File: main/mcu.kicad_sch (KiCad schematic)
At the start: 13 parts, among them J1201 Conn_ARM_JTAG_SWD_20, SW1201 B3SL-1022P, U1201 STM32L476RGTx, Y1201 8MHz

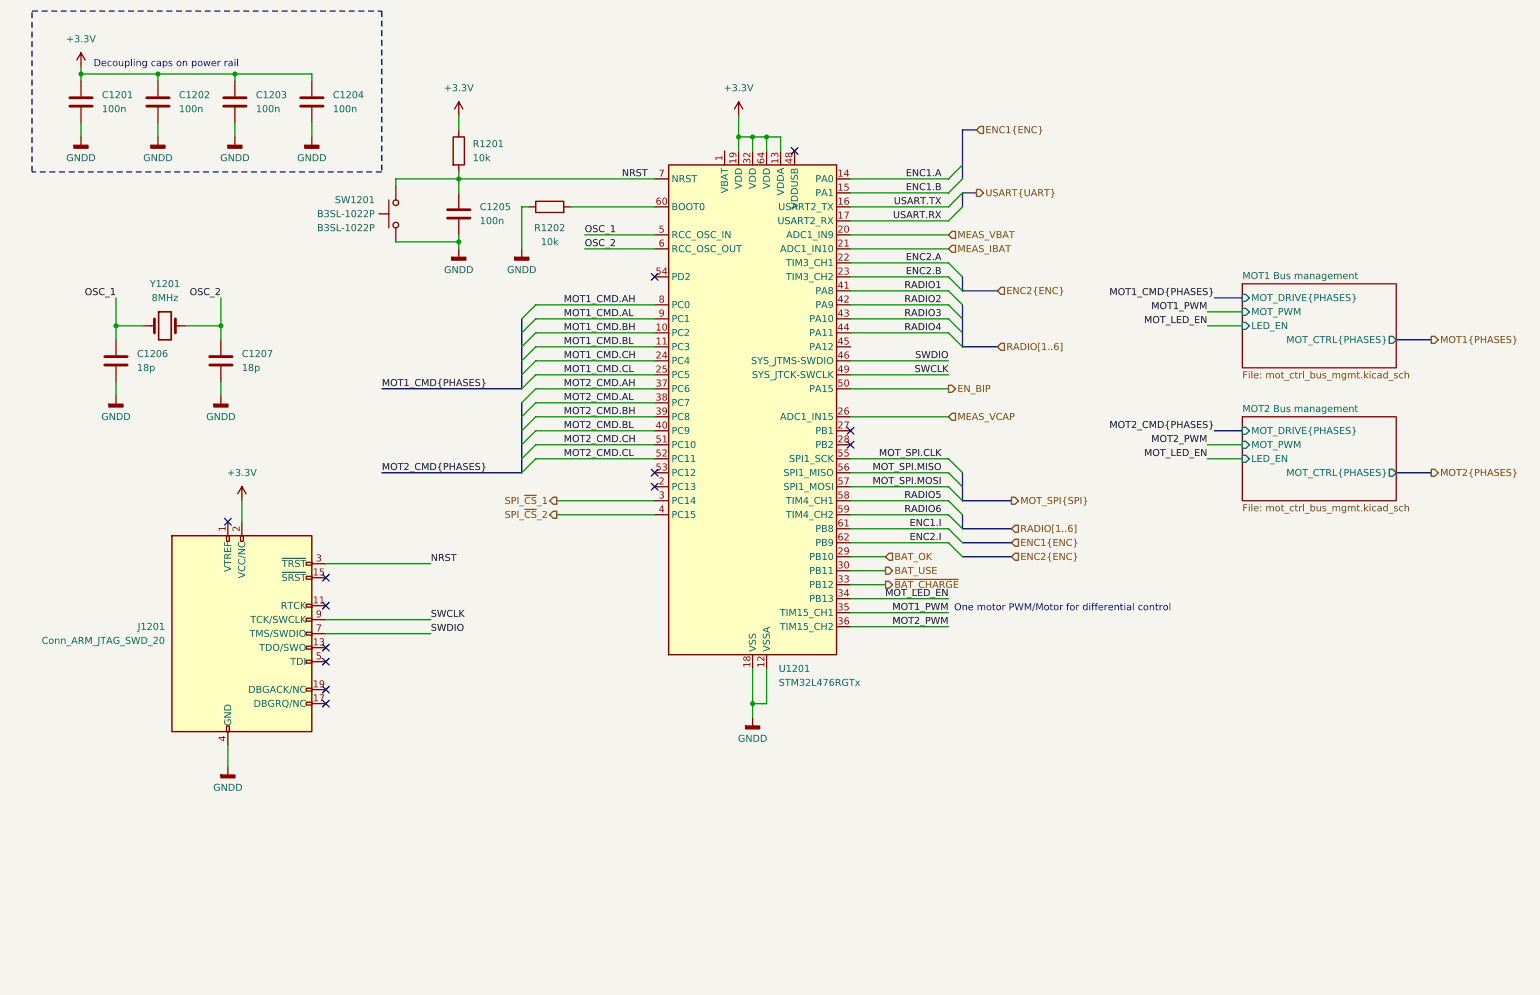
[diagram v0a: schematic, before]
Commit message: Clean silkscreen
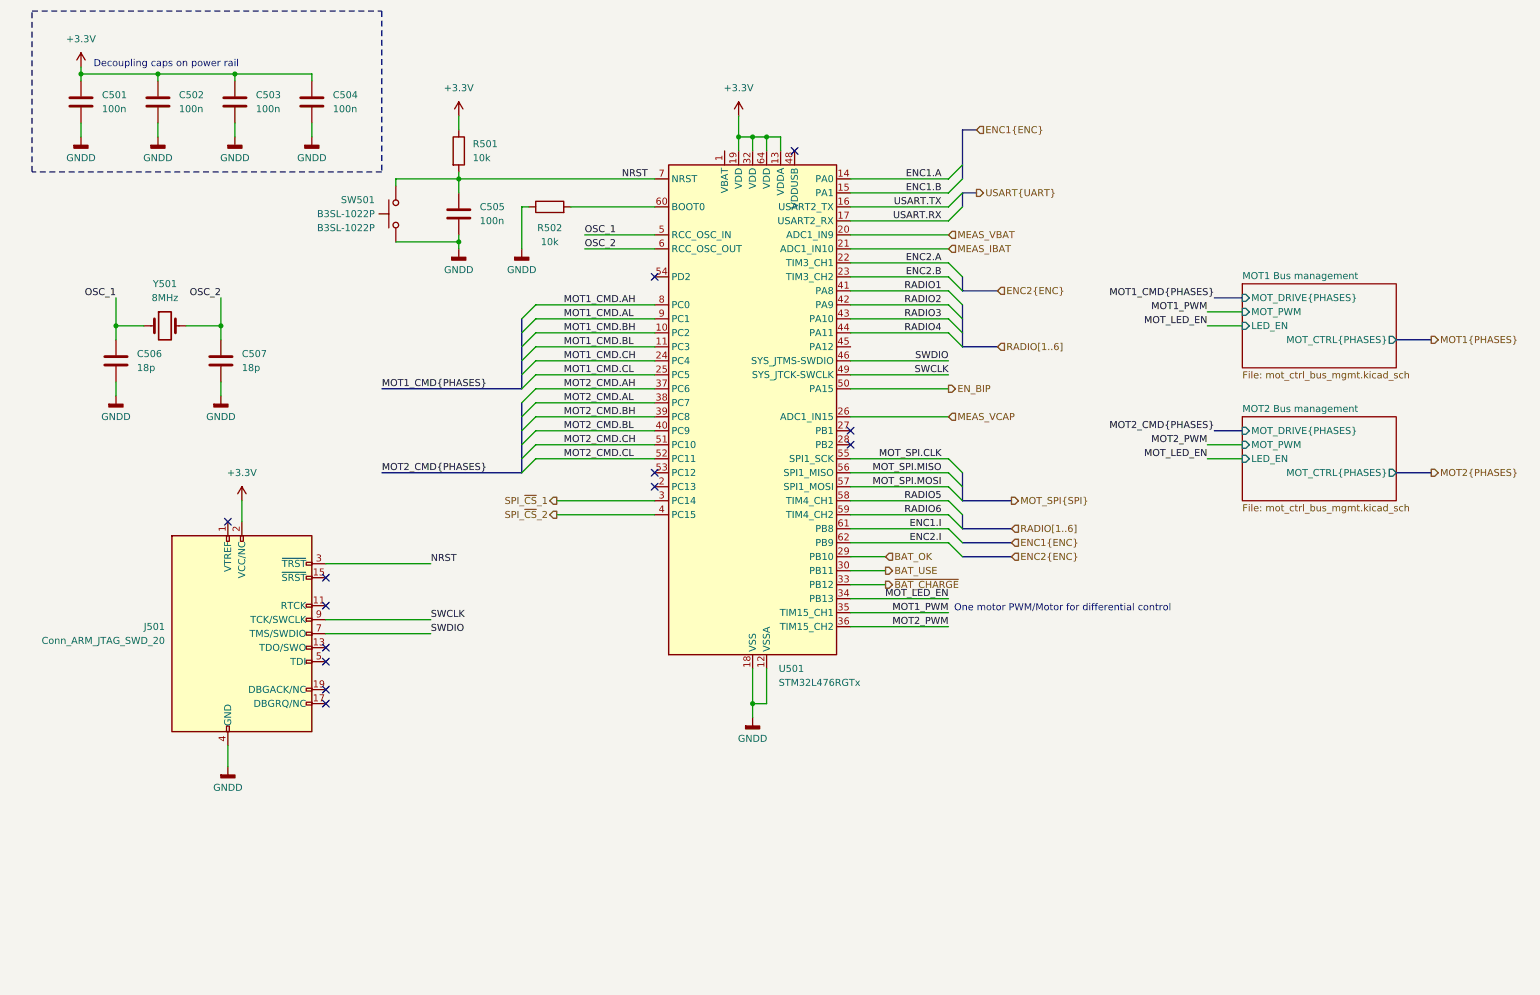
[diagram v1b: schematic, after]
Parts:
- renumbered C1201 to C501, C1202 to C502, C1203 to C503, C1204 to C504, C1205 to C505, C1206 to C506, C1207 to C507, J1201 to J501, R1201 to R501, R1202 to R502, SW1201 to SW501, U1201 to U501, Y1201 to Y501
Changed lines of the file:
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@@
 	(label "ENC2.I"
 		(at 177.8 109.22 180)
+		(fields_autoplaced yes)
 		(effects
 			(font
@@
 	(label "ENC1.I"
 		(at 177.8 106.68 180)
+		(fields_autoplaced yes)
 		(effects
 			(font
@@
 		(dnp no)
 		(fields_autoplaced yes)
-		(property "Reference" "SW1201"
+		(property "Reference" "SW501"
 			(at 74.93 46.9899 90)
 			(effects
@@
 			(project "dsv4"
 				(path "/c07e9297-fde8-4755-803e-d05072cd6096/0865f076-bf0e-442f-8617-d4097538e68b"
-					(reference "SW1201")
+					(reference "SW501")
 					(unit 1)
 				)
@@
 		(dnp no)
 		(fields_autoplaced yes)
-		(property "Reference" "C1204"
+		(property "Reference" "C504"
 			(at 67.31 27.9399 0)
 			(effects
@@
 			(project "dsv4"
 				(path "/c07e9297-fde8-4755-803e-d05072cd6096/0865f076-bf0e-442f-8617-d4097538e68b"
-					(reference "C1204")
+					(reference "C504")
 					(unit 1)
 				)
@@
 		(dnp no)
 		(fields_autoplaced yes)
-		(property "Reference" "#PWR01213"
+		(property "Reference" "#PWR0513"
 			(at 143.51 147.32 0)
 			(effects
@@
 			(project "dsv4"
 				(path "/c07e9297-fde8-4755-803e-d05072cd6096/0865f076-bf0e-442f-8617-d4097538e68b"
-					(reference "#PWR01213")
+					(reference "#PWR0513")
 					(unit 1)
 				)
@@
 		(dnp no)
 		(fields_autoplaced yes)
-		(property "Reference" "#PWR01210"
+		(property "Reference" "#PWR0510"
 			(at 27.94 88.9 0)
 			(effects
@@
 			(project "dsv4"
 				(path "/c07e9297-fde8-4755-803e-d05072cd6096/0865f076-bf0e-442f-8617-d4097538e68b"
-					(reference "#PWR01210")
+					(reference "#PWR0510")
 					(unit 1)
 				)
@@
 		(dnp no)
 		(fields_autoplaced yes)
-		(property "Reference" "#PWR01211"
+		(property "Reference" "#PWR0511"
 			(at 46.99 88.9 0)
 			(effects
@@
 			(project "dsv4"
 				(path "/c07e9297-fde8-4755-803e-d05072cd6096/0865f076-bf0e-442f-8617-d4097538e68b"
-					(reference "#PWR01211")
+					(reference "#PWR0511")
 					(unit 1)
 				)
@@
 		(dnp no)
 		(fields_autoplaced yes)
-		(property "Reference" "C1207"
+		(property "Reference" "C507"
 			(at 50.8 74.9299 0)
 			(effects
@@
 			(project "dsv4"
 				(path "/c07e9297-fde8-4755-803e-d05072cd6096/0865f076-bf0e-442f-8617-d4097538e68b"
-					(reference "C1207")
+					(reference "C507")
 					(unit 1)
 				)
@@
 		(dnp no)
 		(fields_autoplaced yes)
-		(property "Reference" "J1201"
+		(property "Reference" "J501"
 			(at 36.83 124.4599 0)
 			(effects
@@
 			(project "dsv4"
 				(path "/c07e9297-fde8-4755-803e-d05072cd6096/0865f076-bf0e-442f-8617-d4097538e68b"
-					(reference "J1201")
+					(reference "J501")
 					(unit 1)
 				)
@@
 		(dnp no)
 		(fields_autoplaced yes)
-		(property "Reference" "#PWR01209"
+		(property "Reference" "#PWR0509"
 			(at 101.6 62.23 0)
 			(effects
@@
 			(project "dsv4"
 				(path "/c07e9297-fde8-4755-803e-d05072cd6096/0865f076-bf0e-442f-8617-d4097538e68b"
-					(reference "#PWR01209")
+					(reference "#PWR0509")
 					(unit 1)
 				)
@@
 		(dnp no)
 		(fields_autoplaced yes)
-		(property "Reference" "C1206"
+		(property "Reference" "C506"
 			(at 31.75 74.9299 0)
 			(effects
@@
 			(project "dsv4"
 				(path "/c07e9297-fde8-4755-803e-d05072cd6096/0865f076-bf0e-442f-8617-d4097538e68b"
-					(reference "C1206")
+					(reference "C506")
 					(unit 1)
 				)
@@
 		(dnp no)
 		(fields_autoplaced yes)
-		(property "Reference" "R1202"
+		(property "Reference" "R502"
 			(at 106.68 52.07 90)
 			(effects
@@
 			(project "dsv4"
 				(path "/c07e9297-fde8-4755-803e-d05072cd6096/0865f076-bf0e-442f-8617-d4097538e68b"
-					(reference "R1202")
+					(reference "R502")
 					(unit 1)
 				)
@@
 		(dnp no)
 		(fields_autoplaced yes)
-		(property "Reference" "R1201"
+		(property "Reference" "R501"
 			(at 92.71 36.8299 0)
 			(effects
@@
 			(project "dsv4"
 				(path "/c07e9297-fde8-4755-803e-d05072cd6096/0865f076-bf0e-442f-8617-d4097538e68b"
-					(reference "R1201")
+					(reference "R501")
 					(unit 1)
 				)
@@
 		(dnp no)
 		(fields_autoplaced yes)
-		(property "Reference" "#PWR01207"
+		(property "Reference" "#PWR0507"
 			(at 63.5 41.91 0)
 			(effects
@@
 			(project "dsv4"
 				(path "/c07e9297-fde8-4755-803e-d05072cd6096/0865f076-bf0e-442f-8617-d4097538e68b"
-					(reference "#PWR01207")
+					(reference "#PWR0507")
 					(unit 1)
 				)
@@
 		(dnp no)
 		(fields_autoplaced yes)
-		(property "Reference" "#PWR01204"
+		(property "Reference" "#PWR0504"
 			(at 21.59 41.91 0)
 			(effects
@@
 			(project "dsv4"
 				(path "/c07e9297-fde8-4755-803e-d05072cd6096/0865f076-bf0e-442f-8617-d4097538e68b"
-					(reference "#PWR01204")
+					(reference "#PWR0504")
 					(unit 1)
 				)
@@
 		(dnp no)
 		(fields_autoplaced yes)
-		(property "Reference" "#PWR01202"
+		(property "Reference" "#PWR0502"
 			(at 90.17 35.56 0)
 			(effects
@@
 			(project "dsv4"
 				(path "/c07e9297-fde8-4755-803e-d05072cd6096/0865f076-bf0e-442f-8617-d4097538e68b"
-					(reference "#PWR01202")
+					(reference "#PWR0502")
 					(unit 1)
 				)
@@
 		(dnp no)
 		(fields_autoplaced yes)
-		(property "Reference" "#PWR01201"
+		(property "Reference" "#PWR0501"
 			(at 21.59 26.67 0)
 			(effects
@@
 			(project "dsv4"
 				(path "/c07e9297-fde8-4755-803e-d05072cd6096/0865f076-bf0e-442f-8617-d4097538e68b"
-					(reference "#PWR01201")
+					(reference "#PWR0501")
 					(unit 1)
 				)
@@
 		(dnp no)
 		(fields_autoplaced yes)
-		(property "Reference" "#PWR01206"
+		(property "Reference" "#PWR0506"
 			(at 49.53 41.91 0)
 			(effects
@@
 			(project "dsv4"
 				(path "/c07e9297-fde8-4755-803e-d05072cd6096/0865f076-bf0e-442f-8617-d4097538e68b"
-					(reference "#PWR01206")
+					(reference "#PWR0506")
 					(unit 1)
 				)
@@
 		(dnp no)
 		(fields_autoplaced yes)
-		(property "Reference" "C1202"
+		(property "Reference" "C502"
 			(at 39.37 27.9399 0)
 			(effects
@@
 			(project "dsv4"
 				(path "/c07e9297-fde8-4755-803e-d05072cd6096/0865f076-bf0e-442f-8617-d4097538e68b"
-					(reference "C1202")
+					(reference "C502")
 					(unit 1)
 				)
@@
 		(dnp no)
 		(fields_autoplaced yes)
-		(property "Reference" "Y1201"
+		(property "Reference" "Y501"
 			(at 36.83 62.23 0)
 			(effects
@@
 			(project "dsv4"
 				(path "/c07e9297-fde8-4755-803e-d05072cd6096/0865f076-bf0e-442f-8617-d4097538e68b"
-					(reference "Y1201")
+					(reference "Y501")
 					(unit 1)
 				)
@@
 		(dnp no)
 		(fields_autoplaced yes)
-		(property "Reference" "#PWR01214"
+		(property "Reference" "#PWR0514"
 			(at 48.26 156.21 0)
 			(effects
@@
 			(project "dsv4"
 				(path "/c07e9297-fde8-4755-803e-d05072cd6096/0865f076-bf0e-442f-8617-d4097538e68b"
-					(reference "#PWR01214")
+					(reference "#PWR0514")
 					(unit 1)
 				)
@@
 		(dnp no)
 		(fields_autoplaced yes)
-		(property "Reference" "#PWR01212"
+		(property "Reference" "#PWR0512"
 			(at 50.8 105.41 0)
 			(effects
@@
 			(project "dsv4"
 				(path "/c07e9297-fde8-4755-803e-d05072cd6096/0865f076-bf0e-442f-8617-d4097538e68b"
-					(reference "#PWR01212")
+					(reference "#PWR0512")
 					(unit 1)
 				)
@@
 		(dnp no)
 		(fields_autoplaced yes)
-		(property "Reference" "C1205"
+		(property "Reference" "C505"
 			(at 93.98 48.2599 0)
 			(effects
@@
 			(project "dsv4"
 				(path "/c07e9297-fde8-4755-803e-d05072cd6096/0865f076-bf0e-442f-8617-d4097538e68b"
-					(reference "C1205")
+					(reference "C505")
 					(unit 1)
 				)
@@
 		(dnp no)
 		(fields_autoplaced yes)
-		(property "Reference" "#PWR01205"
+		(property "Reference" "#PWR0505"
 			(at 35.56 41.91 0)
 			(effects
@@
 			(project "dsv4"
 				(path "/c07e9297-fde8-4755-803e-d05072cd6096/0865f076-bf0e-442f-8617-d4097538e68b"
-					(reference "#PWR01205")
+					(reference "#PWR0505")
 					(unit 1)
 				)
@@
 		(dnp no)
 		(fields_autoplaced yes)
-		(property "Reference" "U1201"
+		(property "Reference" "U501"
 			(at 148.2441 132.08 0)
 			(effects
@@
 			(project "dsv4"
 				(path "/c07e9297-fde8-4755-803e-d05072cd6096/0865f076-bf0e-442f-8617-d4097538e68b"
-					(reference "U1201")
+					(reference "U501")
 					(unit 1)
 				)
@@
 		(dnp no)
 		(fields_autoplaced yes)
-		(property "Reference" "C1203"
+		(property "Reference" "C503"
 			(at 53.34 27.9399 0)
 			(effects
@@
 			(project "dsv4"
 				(path "/c07e9297-fde8-4755-803e-d05072cd6096/0865f076-bf0e-442f-8617-d4097538e68b"
-					(reference "C1203")
+					(reference "C503")
 					(unit 1)
 				)
@@
 		(dnp no)
 		(fields_autoplaced yes)
-		(property "Reference" "#PWR01208"
+		(property "Reference" "#PWR0508"
 			(at 90.17 62.23 0)
 			(effects
@@
 			(project "dsv4"
 				(path "/c07e9297-fde8-4755-803e-d05072cd6096/0865f076-bf0e-442f-8617-d4097538e68b"
-					(reference "#PWR01208")
+					(reference "#PWR0508")
 					(unit 1)
 				)
@@
 		(dnp no)
 		(fields_autoplaced yes)
-		(property "Reference" "C1201"
+		(property "Reference" "C501"
 			(at 25.4 27.9399 0)
 			(effects
@@
 			(project "dsv4"
 				(path "/c07e9297-fde8-4755-803e-d05072cd6096/0865f076-bf0e-442f-8617-d4097538e68b"
-					(reference "C1201")
+					(reference "C501")
 					(unit 1)
 				)
@@
 		(dnp no)
 		(fields_autoplaced yes)
-		(property "Reference" "#PWR01203"
+		(property "Reference" "#PWR0503"
 			(at 140.97 35.56 0)
 			(effects
@@
 			(project "dsv4"
 				(path "/c07e9297-fde8-4755-803e-d05072cd6096/0865f076-bf0e-442f-8617-d4097538e68b"
-					(reference "#PWR01203")
+					(reference "#PWR0503")
 					(unit 1)
 				)
@@
 			(project "dsv4"
 				(path "/c07e9297-fde8-4755-803e-d05072cd6096/0865f076-bf0e-442f-8617-d4097538e68b"
-					(page "11")
+					(page "16")
 				)
 			)
@@
 			(project "dsv4"
 				(path "/c07e9297-fde8-4755-803e-d05072cd6096/0865f076-bf0e-442f-8617-d4097538e68b"
-					(page "14")
-				)
-			)
+					(page "15")
+				)
+			)

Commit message: Tapeout
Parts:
- added D501: RED, LED_SMD:LED_0805_2012Metric, symbol Device:LED
- added J502: Debug, Connector_IDC:IDC-Header_2x10_P2.54mm_Vertical, symbol Connector_Generic:Conn_02x10_Odd_Even
- added R503: 3k3, Resistor_SMD:R_0805_2012Metric, symbol Device:R
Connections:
- net ENC1.A: now also J502.19 (Pin_19)
- net ENC1.B: now also J502.12 (Pin_12)
- net ENC1.I: now also J502.16 (Pin_16)
- net GNDD: now also D501.1 (K), J502.14 (Pin_14), J502.18 (Pin_18), J502.4 (Pin_4), J502.8 (Pin_8)
- net MOT1_CMD.AH: now also J502.1 (Pin_1)
- net MOT1_CMD.AL: now also J502.3 (Pin_3)
- net MOT1_CMD.BH: now also J502.5 (Pin_5)
- net MOT1_CMD.BL: now also J502.7 (Pin_7)
- net MOT1_CMD.CH: now also J502.9 (Pin_9)
- net MOT1_CMD.CL: now also J502.2 (Pin_2)
- net MOT1_PWM: now also J502.20 (Pin_20)
- net MOT2_CMD.AH: now also J502.6 (Pin_6)
- net MOT2_CMD.AL: now also J502.10 (Pin_10)
- net MOT2_CMD.BH: now also J502.11 (Pin_11)
- net MOT2_CMD.BL: now also J502.13 (Pin_13)
- net MOT2_CMD.CH: now also J502.15 (Pin_15)
- net MOT2_CMD.CL: now also J502.17 (Pin_17)
- net USER_LED: now reaches U501.28 (PB2)
- net USER_LED: now also R503.1
- new net: D501.2 (A), R503.2
- no-connect marks 13 -> 12
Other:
- note added: "DEBUG0"
- note added: "DEBUG1"
- note added: "DEBUG10"
- note added: "DEBUG11"
- note added: "DEBUG12"
- note added: "DEBUG13"
- note added: "DEBUG14"
- note added: "DEBUG15"
- note added: "DEBUG2"
- note added: "DEBUG3"
- note added: "DEBUG4"
- note added: "DEBUG5"
- note added: "DEBUG6"
- note added: "DEBUG7"
- note added: "DEBUG8"
- note added: "DEBUG9"

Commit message: Sent to fab
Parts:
- C501, C502, C503, C504, C505: MPN (none) -> CL21B104KACNFNC; Mouser SKU (none) -> 187-CL21B104KACNFNC
- C506, C507: MPN (none) -> GRM21A5C2J180FWA1D; Mouser SKU (none) -> 81-GRM21A5C2J180FWAD
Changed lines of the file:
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@@
+			)
+		)
+		(property "Quantity" ""
+			(at 78.74 49.53 0)
+			(effects
+				(font
+					(size 1.27 1.27)
+				)
 			)
 		)
@@
 			)
 		)
+		(property "MPN" "CL21B104KACNFNC "
+			(at 63.5 29.21 0)
+			(effects
+				(font
+					(size 1.27 1.27)
+				)
+			)
+		)
+		(property "Mouser SKU" " 187-CL21B104KACNFNC "
+			(at 63.5 29.21 0)
+			(effects
+				(font
+					(size 1.27 1.27)
+				)
+			)
+		)
+		(property "Quantity" ""
+			(at 63.5 29.21 0)
+			(effects
+				(font
+					(size 1.27 1.27)
+				)
+			)
+		)
 		(pin "1"
 		)
@@
 				)
 				(hide yes)
+			)
+		)
+		(property "Quantity" ""
+			(at 241.3 118.11 0)
+			(effects
+				(font
+					(size 1.27 1.27)
+				)
 			)
 		)
@@
 			)
 		)
+		(property "MPN" "GRM21A5C2J180FWA1D"
+			(at 46.99 76.2 0)
+			(effects
+				(font
+					(size 1.27 1.27)
+				)
+			)
+		)
+		(property "Mouser SKU" " 81-GRM21A5C2J180FWAD "
+			(at 46.99 76.2 0)
+			(effects
+				(font
+					(size 1.27 1.27)
+				)
+			)
+		)
+		(property "Quantity" ""
+			(at 46.99 76.2 0)
+			(effects
+				(font
+					(size 1.27 1.27)
+				)
+			)
+		)
 		(pin "1"
 		)
@@
 			)
 		)
+		(property "Quantity" ""
+			(at 50.8 125.73 0)
+			(effects
+				(font
+					(size 1.27 1.27)
+				)
+			)
+		)
 		(pin "8"
 		)
@@
 			)
 		)
+		(property "MPN" "GRM21A5C2J180FWA1D"
+			(at 27.94 76.2 0)
+			(effects
+				(font
+					(size 1.27 1.27)
+				)
+			)
+		)
+		(property "Mouser SKU" " 81-GRM21A5C2J180FWAD "
+			(at 27.94 76.2 0)
+			(effects
+				(font
+					(size 1.27 1.27)
+				)
+			)
+		)
+		(property "Quantity" ""
+			(at 27.94 76.2 0)
+			(effects
+				(font
+					(size 1.27 1.27)
+				)
+			)
+		)
 		(pin "1"
 		)
@@
 			)
 		)
+		(property "Quantity" ""
+			(at 106.68 48.26 0)
+			(effects
+				(font
+					(size 1.27 1.27)
+				)
+			)
+		)
 		(pin "2"
 		)
@@
 			)
 		)
+		(property "Quantity" ""
+			(at 107.95 168.91 0)
+			(effects
+				(font
+					(size 1.27 1.27)
+				)
+			)
+		)
 		(pin "13"
 		)
@@
 			)
 		)
+		(property "Quantity" ""
+			(at 90.17 38.1 0)
+			(effects
+				(font
+					(size 1.27 1.27)
+				)
+			)
+		)
 		(pin "2"
 		)
@@
 			)
 		)
+		(property "MPN" "CL21B104KACNFNC "
+			(at 35.56 29.21 0)
+			(effects
+				(font
+					(size 1.27 1.27)
+				)
+			)
+		)
+		(property "Mouser SKU" " 187-CL21B104KACNFNC "
+			(at 35.56 29.21 0)
+			(effects
+				(font
+					(size 1.27 1.27)
+				)
+			)
+		)
+		(property "Quantity" ""
+			(at 35.56 29.21 0)
+			(effects
+				(font
+					(size 1.27 1.27)
+				)
+			)
+		)
 		(pin "1"
 		)
@@
 			)
 		)
+		(property "Quantity" ""
+			(at 36.83 69.85 0)
+			(effects
+				(font
+					(size 1.27 1.27)
+				)
+			)
+		)
 		(pin "1"
 		)
@@
 			)
 		)
+		(property "MPN" "CL21B104KACNFNC "
+			(at 90.17 49.53 0)
+			(effects
+				(font
+					(size 1.27 1.27)
+				)
+			)
+		)
+		(property "Mouser SKU" " 187-CL21B104KACNFNC "
+			(at 90.17 49.53 0)
+			(effects
+				(font
+					(size 1.27 1.27)
+				)
+			)
+		)
+		(property "Quantity" ""
+			(at 90.17 49.53 0)
+			(effects
+				(font
+					(size 1.27 1.27)
+				)
+			)
+		)
 		(pin "1"
 		)
@@
 			)
 		)
+		(property "Quantity" ""
+			(at 143.51 86.36 0)
+			(effects
+				(font
+					(size 1.27 1.27)
+				)
+			)
+		)
 		(pin "30"
 		)
@@
 			)
 		)
+		(property "MPN" "CL21B104KACNFNC "
+			(at 49.53 29.21 0)
+			(effects
+				(font
+					(size 1.27 1.27)
+				)
+			)
+		)
+		(property "Mouser SKU" " 187-CL21B104KACNFNC "
+			(at 49.53 29.21 0)
+			(effects
+				(font
+					(size 1.27 1.27)
+				)
+			)
+		)
+		(property "Quantity" ""
+			(at 49.53 29.21 0)
+			(effects
+				(font
+					(size 1.27 1.27)
+				)
+			)
+		)
 		(pin "1"
 		)
@@
 			)
 		)
+		(property "Quantity" ""
+			(at 241.3 127 0)
+			(effects
+				(font
+					(size 1.27 1.27)
+				)
+			)
+		)
 		(pin "1"
 		)
@@
 			)
 		)
+		(property "MPN" "CL21B104KACNFNC "
+			(at 21.59 29.21 0)
+			(effects
+				(font
+					(size 1.27 1.27)
+				)
+			)
+		)
+		(property "Mouser SKU" " 187-CL21B104KACNFNC "
+			(at 21.59 29.21 0)
+			(effects
+				(font
+					(size 1.27 1.27)
+				)
+			)
+		)
+		(property "Quantity" ""
+			(at 21.59 29.21 0)
+			(effects
+				(font
+					(size 1.27 1.27)
+				)
+			)
+		)
